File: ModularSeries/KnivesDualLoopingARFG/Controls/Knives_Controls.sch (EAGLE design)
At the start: 19 parts

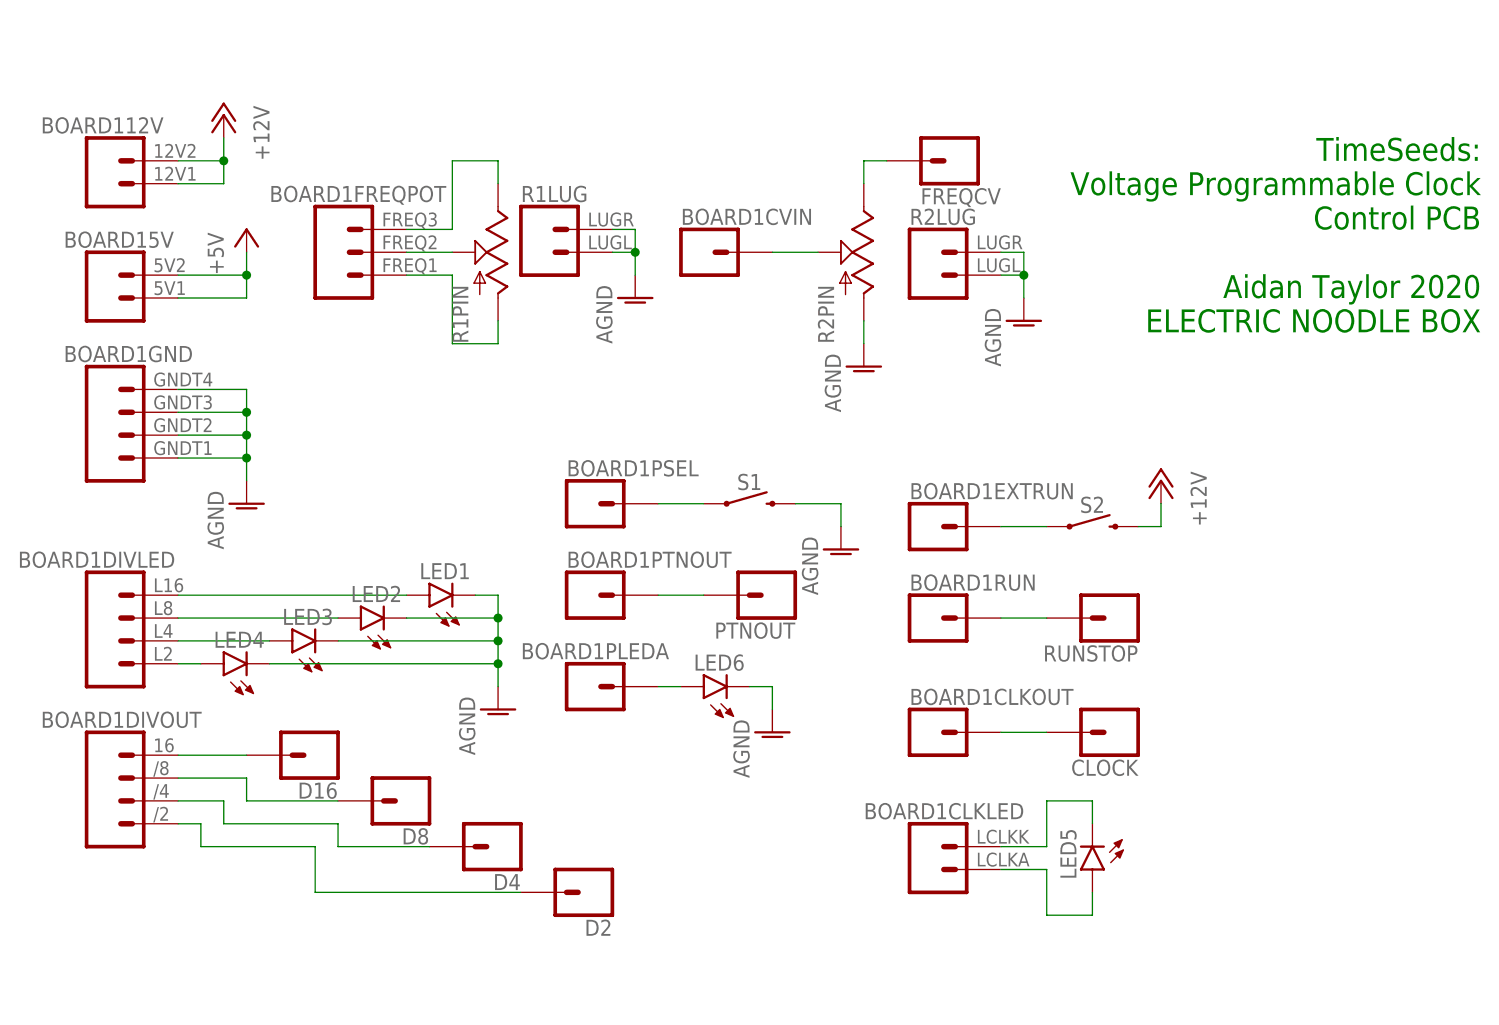
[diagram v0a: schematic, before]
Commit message: Control PCBs for Prism, Portals, TimeSeeds and Knives added
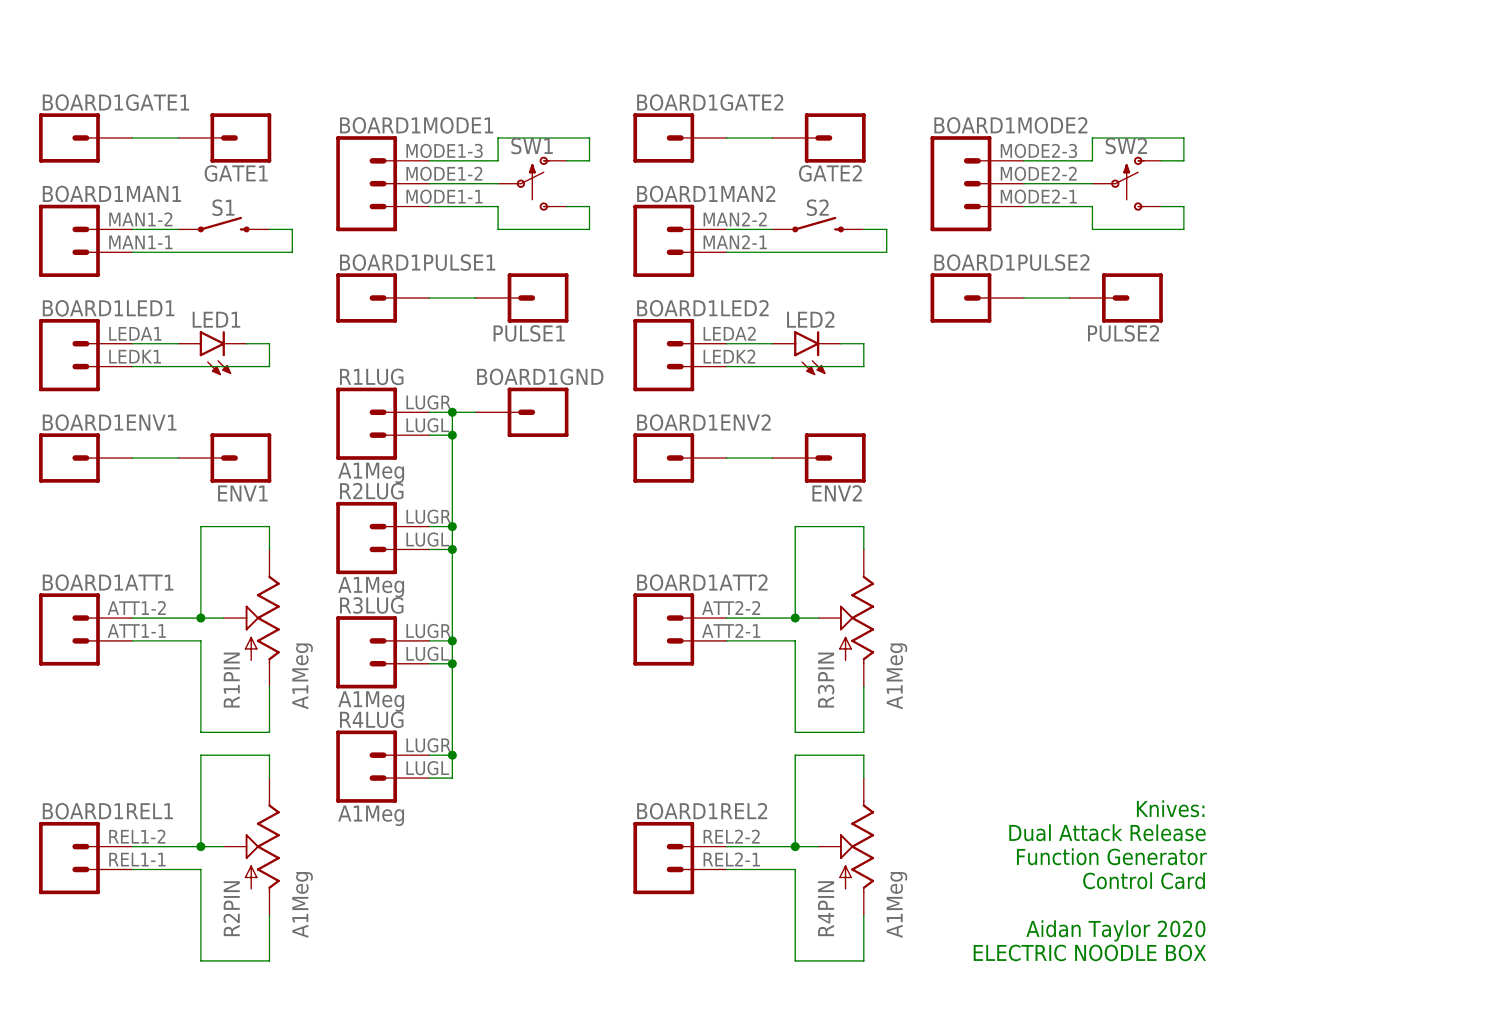
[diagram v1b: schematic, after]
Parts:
- removed CLOCK, D16, D2, D4, D8, FREQCV, PTNOUT, RUNSTOP: BANANA_PANEL, ElectricNoodleBox:BANANA_PANEL
- removed LED3, LED4, LED5, LED6: (no value), led:LED3MM
- added ENV1, ENV2, GATE1, GATE2, PULSE1, PULSE2: BANANA_PANEL, ElectricNoodleBox:BANANA_PANEL
- added R3, R4: A1Meg, ElectricNoodleBox:POTENTIOMETER
- added SW1, SW2: SPDT_SWITCHDW1, ElectricNoodleBox:SPDT_SWITCHDW1
- BOARD1: value TS-VPC_LINK -> KNIVES_LINK; device ElectricNoodleBox:TS-VPC_LINK -> ElectricNoodleBox:KNIVES_LINK
- R1, R2: value (none) -> A1Meg
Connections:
- removed net +12V: BOARD112V.1, BOARD112V.2, S2.2
- removed net +5V: BOARD15V.1, BOARD15V.2
- removed net AGND: BOARD1GND.1, BOARD1GND.2, BOARD1GND.3, BOARD1GND.4, LED1.C, LED2.C, LED3.C, LED4.C, LED6.C, R1LUG.1, R1LUG.2, R2LUG.1, R2LUG.2, R2PIN.A, S1.2
- new net N$22: BOARD1ATT2.1, R3PIN.A
- new net N$23: BOARD1REL2.2, R4PIN.B, R4PIN.W
- new net N$24: BOARD1REL2.1, R4PIN.A
- new net N$25: BOARD1MODE2.1, SW2.S
- new net N$26: BOARD1MODE2.2, SW2.P
- new net N$27: BOARD1MODE2.3, SW2.O
- new net N$28: BOARD1PULSE2.1, PULSE2.1
- new net N$29: BOARD1GND.1, R1LUG.1, R1LUG.2, R2LUG.1, R2LUG.2, R3LUG.1, R3LUG.2, R4LUG.1, R4LUG.2
- net N$1: now also BOARD1GATE1.1, GATE1.1; no longer BOARD1DIVLED.1, LED4.A
- net N$10: now also BOARD1REL1.1, R2PIN.A; no longer BOARD1CLKLED.1, LED5.A
- net N$11: now also BOARD1MODE1.1, SW1.S; no longer BOARD1CLKLED.2, LED5.C
- net N$12: now also BOARD1MODE1.2, SW1.P; no longer BOARD1FREQPOT.2, R1PIN.W
- net N$13: now also BOARD1MODE1.3, SW1.O; no longer BOARD1FREQPOT.1, R1PIN.A
- net N$14: now also BOARD1PULSE1.1, PULSE1.1; no longer BOARD1CVIN.1, R2PIN.W
- net N$15: now also BOARD1GATE2.1, GATE2.1; no longer BOARD1FREQPOT.3, R1PIN.B
- net N$16: now also BOARD1MAN2.2, S2.1; no longer FREQCV.1, R2PIN.B
- net N$17: now also BOARD1MAN2.1, S2.2; no longer BOARD1PTNOUT.1, PTNOUT.1
- net N$18: now also BOARD1LED2.2, LED2.A; no longer BOARD1PLEDA.1, LED6.A
- net N$19: now also BOARD1LED2.1, LED2.C; no longer BOARD1PSEL.1, S1.1
- net N$2: now also BOARD1MAN1.2, S1.1; no longer BOARD1DIVLED.2, LED3.A
- net N$20: now also BOARD1ENV2.1, ENV2.1; no longer BOARD1EXTRUN.1, S2.1
- net N$21: now also BOARD1ATT2.2, R3PIN.B, R3PIN.W; no longer BOARD1RUN.1, RUNSTOP.1
- net N$3: now also BOARD1MAN1.1, S1.2; no longer BOARD1DIVLED.3, LED2.A
- net N$4: now also BOARD1LED1.2; no longer BOARD1DIVLED.4
- net N$5: now also BOARD1LED1.1, LED1.C; no longer BOARD1DIVOUT.4, D16.1
- net N$6: now also BOARD1ENV1.1, ENV1.1; no longer BOARD1DIVOUT.3, D8.1
- net N$7: now also BOARD1ATT1.2, R1PIN.B, R1PIN.W; no longer BOARD1DIVOUT.2, D4.1
- net N$8: now also BOARD1ATT1.1, R1PIN.A; no longer BOARD1DIVOUT.1, D2.1
- net N$9: now also BOARD1REL1.2, R2PIN.B, R2PIN.W; no longer BOARD1CLKOUT.1, CLOCK.1
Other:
- note added: "Knives: Dual Attack Release Function Generator Control Card Aidan Taylor 2020 ELECTRIC NOODLE BOX"
- note removed: "TimeSeeds: Voltage Programmable Clock Control PCB Aidan Taylor 2020 ELECTRIC NOODLE BOX"
- moved on the sheet: LED1, LED2, R1LUG, R1PIN, R2LUG, R2PIN, S1, S2

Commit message: Updates to Portals and Knives, Panel layout for Prism and Knives added
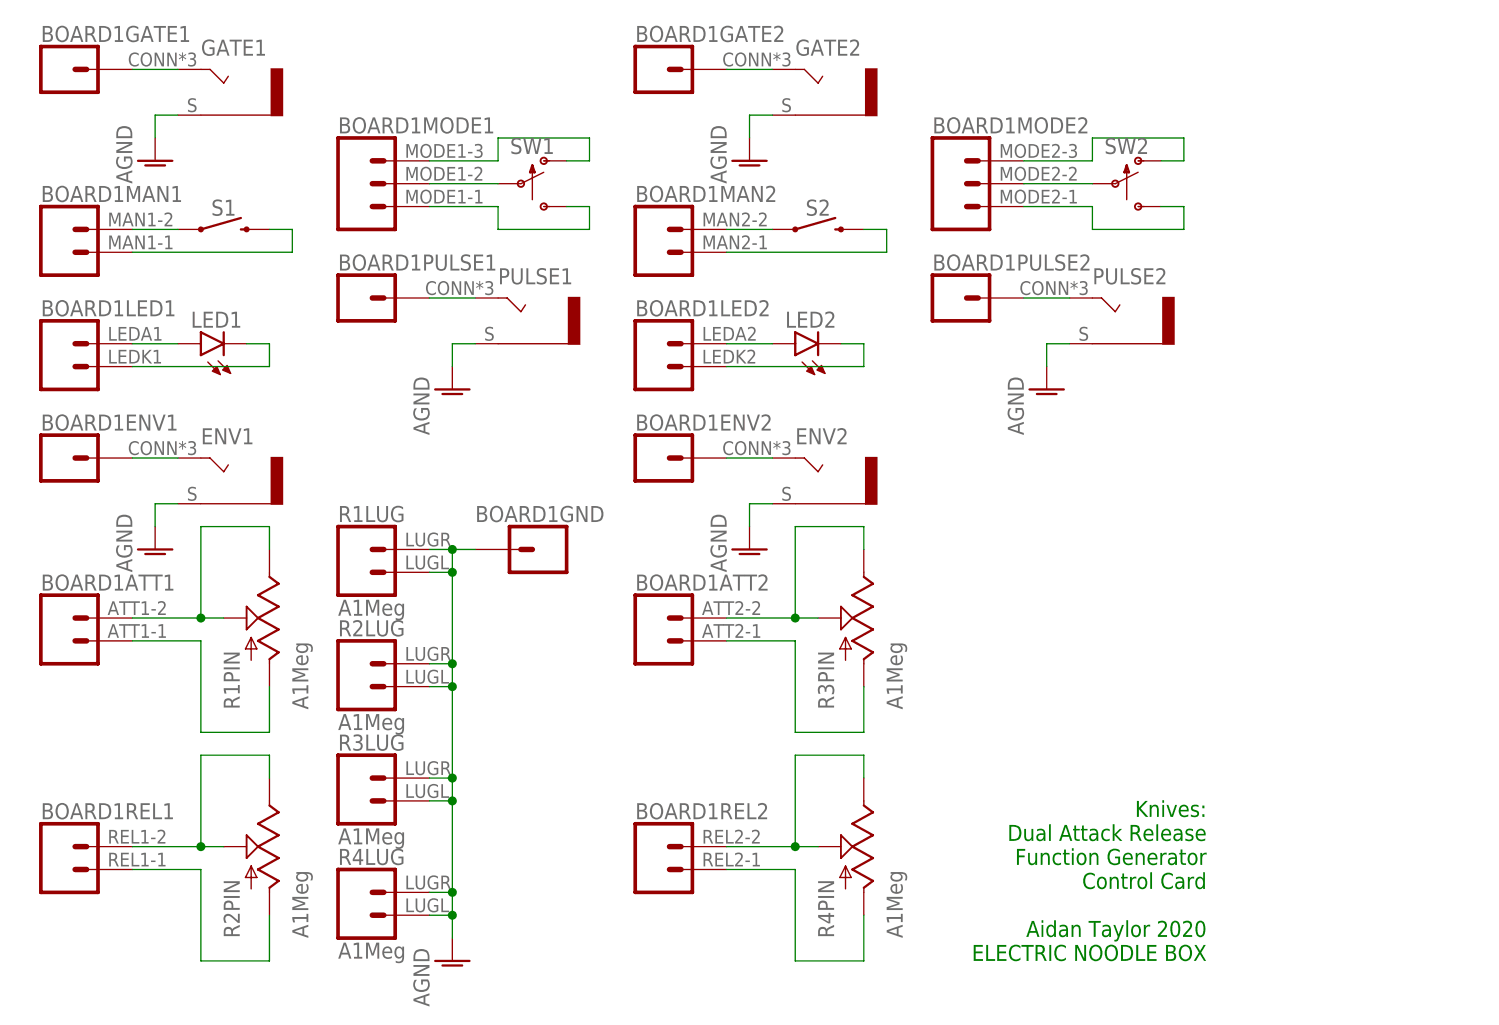
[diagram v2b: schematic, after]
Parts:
- ENV1, ENV2, GATE1, GATE2, PULSE1, PULSE2: value BANANA_PANEL -> COMBI-JACKCINCHNANA; device ElectricNoodleBox:BANANA_PANEL -> ElectricNoodleBox:COMBI-JACKCINCHNANA
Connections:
- removed net N$29: BOARD1GND.1, R1LUG.1, R1LUG.2, R2LUG.1, R2LUG.2, R3LUG.1, R3LUG.2, R4LUG.1, R4LUG.2
- new net AGND: BOARD1GND.1, ENV1.S, ENV2.S, GATE1.S, GATE2.S, PULSE1.S, PULSE2.S, R1LUG.1, R1LUG.2, R2LUG.1, R2LUG.2, R3LUG.1, R3LUG.2, R4LUG.1, R4LUG.2
- net N$1: now also GATE1.T; no longer GATE1.1
- net N$14: now also PULSE1.T; no longer PULSE1.1
- net N$15: now also GATE2.T; no longer GATE2.1
- net N$20: now also ENV2.T; no longer ENV2.1
- net N$28: now also PULSE2.T; no longer PULSE2.1
- net N$6: now also ENV1.T; no longer ENV1.1
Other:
- moved on the sheet: BOARD1GATE1, BOARD1GATE2, BOARD1GND, R1LUG, R2LUG, R3LUG, R4LUG
